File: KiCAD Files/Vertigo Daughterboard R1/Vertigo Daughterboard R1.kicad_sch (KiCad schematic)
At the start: 21 parts, among them J1 Conn_01x08_Pin, U1 ICM-20602, U1 NEO-6M-GPS, U2 24AA32A-I_MS, U2 DPS310XTSA1

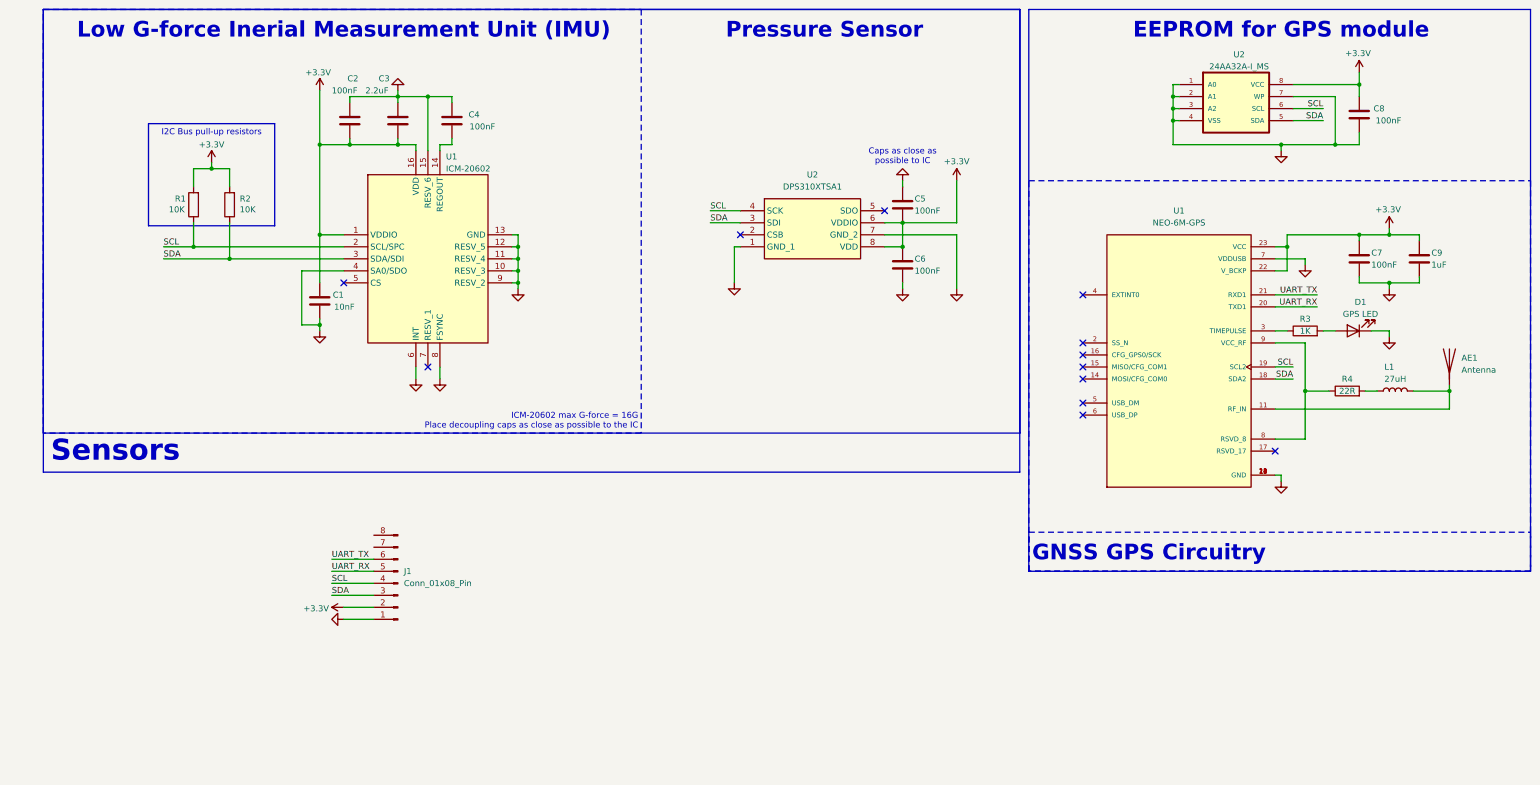
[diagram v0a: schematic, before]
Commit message: switched I2C to SPI, new PCB shape, fix for BOM
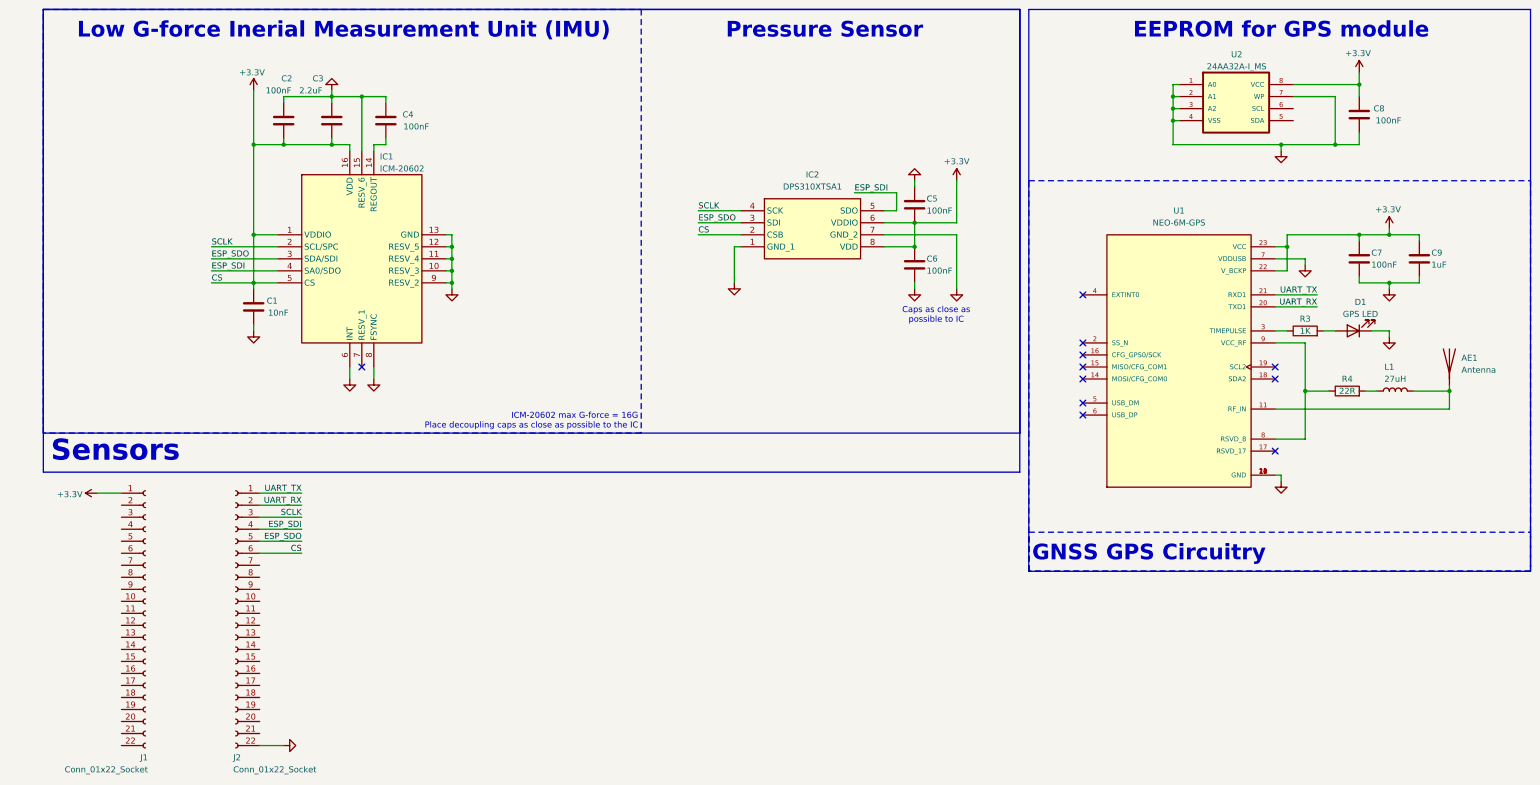
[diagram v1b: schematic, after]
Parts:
- removed J1: Conn_01x08_Pin, Connector_PinHeader_2.54mm:PinHeader_1x08_P2.54mm_Vertical, symbol Connector:Conn_01x08_Pin
- removed R1, R2: 10K, Resistor_SMD:R_0805_2012Metric, symbol Device:R
- added J1, J2: Conn_01x22_Socket, Connector_PinHeader_2.54mm:PinHeader_1x22_P2.54mm_Vertical, symbol Connector:Conn_01x22_Socket
- renumbered U1 to IC1, U2 to IC2
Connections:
- net +3.3V: now also IC1.5 (CS), IC2.2 (CSB), J1.1 (Pin_1), J2.6 (Pin_6)
- net GND: now also J2.22 (Pin_22); no longer IC1.4 (SA0/SDO)
- net UART_RX: now also J2.2 (Pin_2)
- net UART_TX: now also J2.1 (Pin_1)
- net ESP_SDI: now reaches IC2.5 (SDO)
- net ESP_SDI: now also IC1.4 (SA0/SDO), J2.4 (Pin_4)
- net SCL renamed SCLK
- net SCLK: now also J2.3 (Pin_3); no longer U1.19 (SCL2), U2.6 (SCL)
- net SDA renamed ESP_SDO
- net ESP_SDO: now also J2.5 (Pin_5); no longer U1.18 (SDA2), U2.5 (SDA)
- no-connect marks 12 -> 11
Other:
- note removed: "I2C Bus pull-up resistors"
- moved on the sheet: C1, C2, C3, C4, C5, C6, IC1

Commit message: note
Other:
- note added: "zmienić"
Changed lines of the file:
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@@
+		)
+	)
+	(text "zmienić"
+		(exclude_from_sim no)
+		(at 265.938 45.212 0)
+		(effects
+			(font
+				(size 1.27 1.27)
+				(color 255 0 0 1)
+			)
 		)
 	)

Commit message: note 2
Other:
- note added: "sprawdzić połączenie"
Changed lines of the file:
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@@
+		)
+	)
+	(text "sprawdzić połączenie"
+		(exclude_from_sim no)
+		(at 45.466 75.184 0)
+		(effects
+			(font
+				(size 1.27 1.27)
+				(thickness 0.254)
+				(bold yes)
+				(color 255 0 0 1)
+			)
 		)
 	)
